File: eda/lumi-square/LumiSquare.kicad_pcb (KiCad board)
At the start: 2 copper layers, 100 x 100 mm, 70 parts, among them J1 Conn_01x02, J2 Conn_01x02, J3 Conn_01x02, J4 Conn_01x02, J5 USB_C_Receptacle_USB2.0, J6 Conn_01x04, J7 Conn_01x04, J8 Conn_01x04, J9 Conn_01x04, Q1 Q_PMOS_GSD, Q2 Q_PMOS_GSD, Q3 Q_PMOS_GSD, Q4 Q_PMOS_GSD, Q5 MMBT3904, Q6 MMBT3904, Q7 MMBT3904, Q8 MMBT3904, U1 MCP2200-I-SO, U2 ATmega1284-A, U3 ATtiny861A-S, U4 STP16CPC05MTR, U5 TPS3840, U6 TPS3840

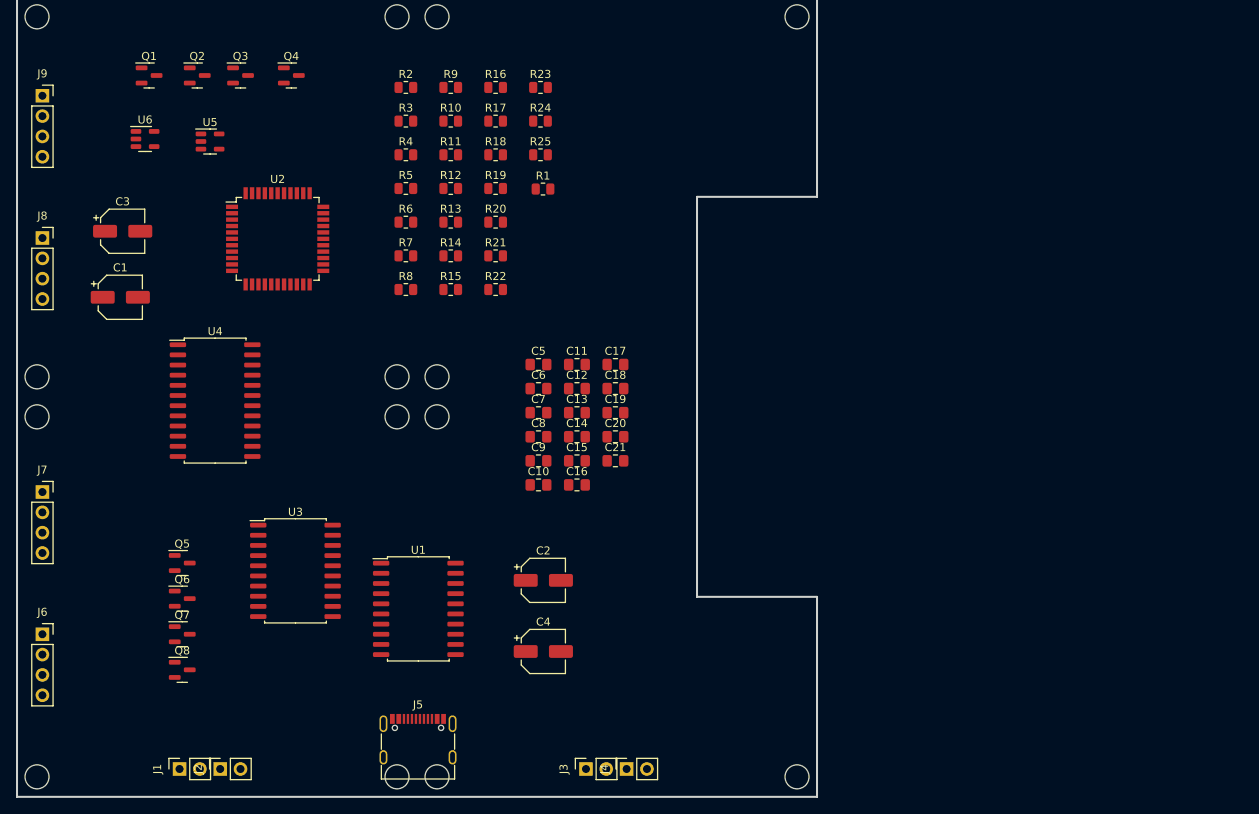
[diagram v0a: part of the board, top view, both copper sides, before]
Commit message: - Connected power portion of the schmatic - added components to the pcb editor
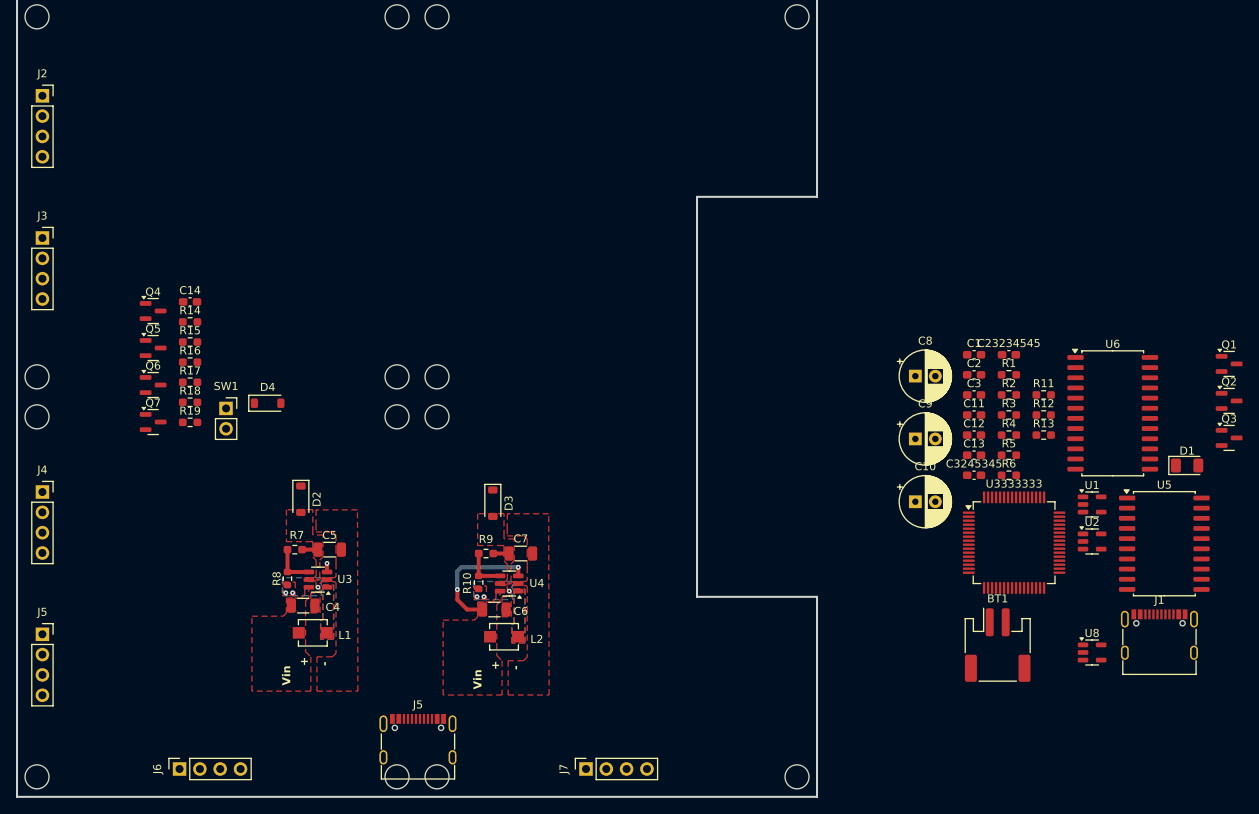
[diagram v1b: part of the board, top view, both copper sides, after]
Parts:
- removed C15, C16, C17, C18, C19, C20, C21: C, Capacitor_SMD:C_0805_2012Metric_Pad1.18x1.45mm_HandSolder
- removed the J2 at (121.9, 136.2)
- removed the J3 at (167.6, 136.2)
- removed the J4 at (172.7, 136.2)
- removed Q8: MMBT3904, Package_TO_SOT_SMD:SOT-23
- removed R20, R21, R22, R23, R24, R25: R, Resistor_SMD:R_0805_2012Metric
- added BT1: 4.2V Lipo, Connector_JST:JST_PH_S2B-PH-SM4-TB_1x02-1MP_P2.00mm_Horizontal, F.Cu at (219.1, 120.7)
- added C23234545: 1uF, Capacitor_SMD:C_0603_1608Metric_Pad1.08x0.95mm_HandSolder, F.Cu at (220.5, 84.4)
- added C3245345: 2.2uF, Capacitor_SMD:C_0603_1608Metric_Pad1.08x0.95mm_HandSolder, F.Cu at (216.2, 99.5)
- added D1: LED, LED_SMD:LED_1206_3216Metric, F.Cu at (242.8, 98.3)
- added D2: 1N5819HW-7-F, Diode_SMD:D_SOD-123, F.Cu at (132.0, 102.5)
- added D3: 1N5819HW-7-F, Diode_SMD:D_SOD-123, F.Cu at (156.0, 103.0)
- added D4: 1N4148W, Diode_SMD:D_SOD-123, F.Cu at (127.8, 90.5)
- added J6: Conn_01x04, Connector_PinSocket_2.54mm:PinSocket_1x04_P2.54mm_Vertical, F.Cu at (116.8, 136.2)
- added J7: Conn_01x04, Connector_PinSocket_2.54mm:PinSocket_1x04_P2.54mm_Vertical, F.Cu at (167.6, 136.2)
- added L1: 4.7uH, InductorCustom:Bourns SRP30xx, F.Cu at (133.5, 119.2)
- added L2: 4.7uH, InductorCustom:Bourns SRP30xx, F.Cu at (157.4, 119.7)
- added SW1: SW_Push, Connector_PinSocket_2.54mm:PinSocket_1x02_P2.54mm_Vertical, F.Cu at (122.7, 91.2)
- added U3333333: ATSAMD21J18A-A, Package_QFP:TQFP-64_10x10mm_P0.5mm, F.Cu at (221.2, 107.9)
- added U8: MIC5225-3.3YM5, Package_TO_SOT_SMD:SOT-23-5, F.Cu at (230.9, 121.7)
- C1, C2: value C_Polarized_US -> 4.7uF; footprint Capacitor_SMD:CP_Elec_5x5.3 -> Capacitor_SMD:C_0603_1608Metric_Pad1.08x0.95mm_HandSolder
- C10, C8, C9: value C -> 100uF; footprint Capacitor_SMD:C_0805_2012Metric_Pad1.18x1.45mm_HandSolder -> Capacitor_THT:CP_Radial_D6.3mm_P2.50mm
- C11, C12, C13, C14: value C -> .1uF; footprint Capacitor_SMD:C_0805_2012Metric_Pad1.18x1.45mm_HandSolder -> Capacitor_SMD:C_0603_1608Metric_Pad1.08x0.95mm_HandSolder
- C3: value C_Polarized_US -> 1uF; footprint Capacitor_SMD:CP_Elec_5x5.3 -> Capacitor_SMD:C_0603_1608Metric_Pad1.08x0.95mm_HandSolder
- C4: value C_Polarized_US -> 10uF; footprint Capacitor_SMD:CP_Elec_5x5.3 -> Capacitor_SMD:C_1206_3216Metric
- C5, C7: value C -> 22uF; footprint Capacitor_SMD:C_0805_2012Metric_Pad1.18x1.45mm_HandSolder -> Capacitor_SMD:C_1206_3216Metric
- C6: value C -> 10uF; footprint Capacitor_SMD:C_0805_2012Metric_Pad1.18x1.45mm_HandSolder -> Capacitor_SMD:C_1206_3216Metric
- J1: value Conn_01x02 -> USB_C_Receptacle_USB2.0_14P; footprint Connector_PinSocket_2.54mm:PinSocket_1x02_P2.54mm_Vertical -> Connector_USB:USB_C_Receptacle_G-Switch_GT-USB-7010ASV
- Q1: value Q_PMOS_GSD -> IRLML6244
- Q2, Q4: value Q_PMOS_GSD -> MMBT3904
- Q3: value Q_PMOS_GSD -> IRLML2246
- R1, R2: value R -> 5.1k; footprint Resistor_SMD:R_0805_2012Metric -> Resistor_SMD:R_0603_1608Metric_Pad0.98x0.95mm_HandSolder
- R10, R8: value R -> 80k; footprint Resistor_SMD:R_0805_2012Metric -> Resistor_SMD:R_0603_1608Metric
- R11: value R -> 300; footprint Resistor_SMD:R_0805_2012Metric -> Resistor_SMD:R_0603_1608Metric_Pad0.98x0.95mm_HandSolder
- R12: value R -> 100k; footprint Resistor_SMD:R_0805_2012Metric -> Resistor_SMD:R_0603_1608Metric_Pad0.98x0.95mm_HandSolder
- R13, R3: value R -> 10k; footprint Resistor_SMD:R_0805_2012Metric -> Resistor_SMD:R_0603_1608Metric_Pad0.98x0.95mm_HandSolder
- R14, R15: value R -> 200k; footprint Resistor_SMD:R_0805_2012Metric -> Resistor_SMD:R_0603_1608Metric_Pad0.98x0.95mm_HandSolder
- R16, R17, R18, R19: value R -> 2.2k; footprint Resistor_SMD:R_0805_2012Metric -> Resistor_SMD:R_0603_1608Metric_Pad0.98x0.95mm_HandSolder
- R4: value R -> 330; footprint Resistor_SMD:R_0805_2012Metric -> Resistor_SMD:R_0603_1608Metric_Pad0.98x0.95mm_HandSolder
- R5: value R -> 1.3k; footprint Resistor_SMD:R_0805_2012Metric -> Resistor_SMD:R_0603_1608Metric_Pad0.98x0.95mm_HandSolder
- R6: value R -> 150k; footprint Resistor_SMD:R_0805_2012Metric -> Resistor_SMD:R_0603_1608Metric_Pad0.98x0.95mm_HandSolder
- R7, R9: value R -> 720k; footprint Resistor_SMD:R_0805_2012Metric -> Resistor_SMD:R_0603_1608Metric_Pad0.98x0.95mm_HandSolder
- U1: value MCP2200-I-SO -> MCP73831-2-OT; footprint Package_SO:SOIC-20W_7.5x12.8mm_P1.27mm -> Package_TO_SOT_SMD:SOT-23-5
- U2: value ATmega1284-A -> TPS3840; footprint Package_QFP:TQFP-44_10x10mm_P0.8mm -> Package_TO_SOT_SMD:SOT-23-5
- U3: value ATtiny861A-S -> TLV61070A; footprint Package_SO:SOIC-20W_7.5x12.8mm_P1.27mm -> Package_TO_SOT_SMD:SOT-23-6
- U4: value STP16CPC05MTR -> TLV61070A; footprint Package_SO:SOIC-24W_7.5x15.4mm_P1.27mm -> Package_TO_SOT_SMD:SOT-23-6
- U5: value TPS3840 -> ATtiny861A-S; footprint Package_TO_SOT_SMD:SOT-23-5 -> Package_SO:SOIC-20W_7.5x12.8mm_P1.27mm
- U6: value TPS3840 -> STP16CPC05MTR; footprint Package_TO_SOT_SMD:SOT-23-5 -> Package_SO:SOIC-24W_7.5x15.4mm_P1.27mm
- moved Q1 139.7 mm to (248.0, 85.6)
- moved Q2 135.3 mm to (248.0, 90.2)
- moved Q3 131.6 mm to (248.0, 94.8)
- moved U5 129.4 mm to (239.9, 108.1)
- moved U6 125.7 mm to (233.5, 91.8)
- moved J1 123.5 mm to (239.3, 120.6), turned to 0 degrees
- moved U2 108.6 mm to (230.9, 107.8)
- moved C3 108.4 mm to (216.2, 89.5)
- moved C1 107.0 mm to (216.2, 84.4)
- moved U1 85.2 mm to (230.9, 103.2)
- moved R2 84.6 mm to (220.5, 89.5)
- moved R3 83.9 mm to (220.5, 92.0)
- moved R4 83.1 mm to (220.5, 94.5)
- moved R5 82.4 mm to (220.5, 97.0)
- moved R6 81.7 mm to (220.5, 99.5)
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- renumbered J6 to J2, J7 to J3, J8 to J4, J9 to J5
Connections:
- C1 pad 1: unconnected-(C1-Pad1) -> /5V USB
- C1 pad 2: unconnected-(C1-Pad2) -> GNDREF
- C10 pad 1: unconnected-(C10-Pad1) -> /5.3V Out
- C10 pad 2: unconnected-(C10-Pad2) -> GNDREF
- C11 pad 1: unconnected-(C11-Pad1) -> /5.3V Out
- C11 pad 2: unconnected-(C11-Pad2) -> GNDREF
- C12 pad 1: unconnected-(C12-Pad1) -> /5.3V Out
- C12 pad 2: unconnected-(C12-Pad2) -> GNDREF
- C13 pad 1: unconnected-(C13-Pad1) -> /AREF
- C13 pad 2: unconnected-(C13-Pad2) -> GNDREF
- C14 pad 1: unconnected-(C14-Pad1) -> /PB7
- C14 pad 2: unconnected-(C14-Pad2) -> GNDREF
- C2 pad 1: unconnected-(C2-Pad1) -> /4.2V Bat
- C2 pad 2: unconnected-(C2-Pad2) -> GNDREF
- C3 pad 1: unconnected-(C3-Pad1) -> /4.2V Bat
- C3 pad 2: unconnected-(C3-Pad2) -> GNDREF
- C4 pad 1: unconnected-(C4-Pad1) -> GNDREF
- C4 pad 2: unconnected-(C4-Pad2) -> /4.2V Bat
- C5 pad 1: unconnected-(C5-Pad1) -> Net-(D2-A)
- C5 pad 2: unconnected-(C5-Pad2) -> GNDREF
- C6 pad 1: unconnected-(C6-Pad1) -> /5V USB
- C6 pad 2: unconnected-(C6-Pad2) -> GNDREF
- C7 pad 1: unconnected-(C7-Pad1) -> Net-(D3-A)
- C7 pad 2: unconnected-(C7-Pad2) -> GNDREF
- C8 pad 1: unconnected-(C8-Pad1) -> /5.3V Out
- C8 pad 2: unconnected-(C8-Pad2) -> GNDREF
- C9 pad 1: unconnected-(C9-Pad1) -> /5.3V Out
- C9 pad 2: unconnected-(C9-Pad2) -> GNDREF
- J2 pad 2: unconnected-(J6-Pin_2-Pad2) -> /LED1
- J2 pad 3: unconnected-(J6-Pin_3-Pad3) -> /LED2
- J2 pad 4: unconnected-(J6-Pin_4-Pad4) -> /LED3
- J3 pad 2: unconnected-(J7-Pin_2-Pad2) -> /LED4
- J3 pad 3: unconnected-(J7-Pin_3-Pad3) -> /LED5
- J3 pad 4: unconnected-(J7-Pin_4-Pad4) -> /LED6
- J4 pad 2: unconnected-(J8-Pin_2-Pad2) -> /LED7
- J4 pad 3: unconnected-(J8-Pin_3-Pad3) -> /LED8
- J4 pad 4: unconnected-(J8-Pin_4-Pad4) -> /LED9
- J5 pad 2: unconnected-(J9-Pin_2-Pad2) -> /LED10
- J5 pad 3: unconnected-(J9-Pin_3-Pad3) -> /LED11
- J5 pad 4: unconnected-(J9-Pin_4-Pad4) -> /LED12
- Q1 pad 1: unconnected-(Q1-G-Pad1) -> /5V USB
- Q1 pad 2: unconnected-(Q1-S-Pad2) -> GNDREF
- Q1 pad 3: unconnected-(Q1-D-Pad3) -> Net-(Q1-D)
- Q2 pad 1: unconnected-(Q2-G-Pad1) -> Net-(Q2-B)
- Q2 pad 2: unconnected-(Q2-S-Pad2) -> GNDREF
- Q2 pad 3: unconnected-(Q2-D-Pad3) -> Net-(Q2-C)
- Q3 pad 1: unconnected-(Q3-G-Pad1) -> Net-(Q2-C)
- Q3 pad 2: unconnected-(Q3-S-Pad2) -> /5.3V Out
- Q3 pad 3: unconnected-(Q3-D-Pad3) -> Net-(Q3-D)
- R1 pad 1: unconnected-(R1-Pad1) -> Net-(J1-CC2)
- R1 pad 2: unconnected-(R1-Pad2) -> GNDREF
- R10 pad 1: unconnected-(R10-Pad1) -> Net-(U4-FB)
- R10 pad 2: unconnected-(R10-Pad2) -> GNDREF
- R11 pad 1: unconnected-(R11-Pad1) -> Net-(U5-PA7)
- R11 pad 2: unconnected-(R11-Pad2) -> Net-(Q2-B)
- R12 pad 1: unconnected-(R12-Pad1) -> Net-(U5-PA7)
- R12 pad 2: unconnected-(R12-Pad2) -> GNDREF
- R13 pad 1: unconnected-(R13-Pad1) -> /5.3V Out
- R13 pad 2: unconnected-(R13-Pad2) -> Net-(Q2-C)
- R14 pad 1: unconnected-(R14-Pad1) -> /5.3V Out
- R14 pad 2: unconnected-(R14-Pad2) -> /PB6
- R15 pad 1: unconnected-(R15-Pad1) -> /5.3V Out
- R15 pad 2: unconnected-(R15-Pad2) -> /PB7
- R2 pad 1: unconnected-(R2-Pad1) -> Net-(J1-CC1)
- R2 pad 2: unconnected-(R2-Pad2) -> GNDREF
- R3 pad 1: unconnected-(R3-Pad1) -> Net-(U1-PROG)
- R3 pad 2: unconnected-(R3-Pad2) -> GNDREF
- R4 pad 1: unconnected-(R4-Pad1) -> /5V USB
- R4 pad 2: unconnected-(R4-Pad2) -> Net-(D1-A)
- R5 pad 1: unconnected-(R5-Pad1) -> /5V USB
- R5 pad 2: unconnected-(R5-Pad2) -> GNDREF
- R6 pad 1: unconnected-(R6-Pad1) -> /4.2V Bat
- R6 pad 2: unconnected-(R6-Pad2) -> Net-(Q1-D)
- R7 pad 1: unconnected-(R7-Pad1) -> Net-(D2-A)
- R7 pad 2: unconnected-(R7-Pad2) -> Net-(U3-FB)
- R8 pad 1: unconnected-(R8-Pad1) -> Net-(U3-FB)
- R8 pad 2: unconnected-(R8-Pad2) -> GNDREF
- R9 pad 1: unconnected-(R9-Pad1) -> Net-(D3-A)
- R9 pad 2: unconnected-(R9-Pad2) -> Net-(U4-FB)
- U1 pad 1: unconnected-(U1-VDD-Pad1) -> Net-(D1-K)
- U1 pad 2: unconnected-(U1-OSC1-Pad2) -> GNDREF
- U1 pad 3: unconnected-(U1-OSC2-Pad3) -> /4.2V Bat
- U1 pad 4: unconnected-(U1-RST-Pad4) -> /5V USB
- U1 pad 5: unconnected-(U1-GP7/TxLED-Pad5) -> Net-(U1-PROG)
- U2 pad 1: unconnected-(U2-PB5-Pad1) -> Net-(Q1-D)
- U2 pad 2: unconnected-(U2-PB6-Pad2) -> /4.2V Bat
- U2 pad 3: unconnected-(U2-PB7-Pad3) -> GNDREF
- U2 pad 5: Net-(U2-VCC-Pad17) -> unconnected-(U2-CT-Pad5)
- U3 pad 1: unconnected-(U3-PB0-Pad1) -> Net-(U3-SW)
- U3 pad 2: unconnected-(U3-PB1-Pad2) -> GNDREF
- U3 pad 3: unconnected-(U3-PB2-Pad3) -> Net-(Q1-D)
- U3 pad 4: unconnected-(U3-PB3-Pad4) -> Net-(U3-FB)
- U3 pad 5: unconnected-(U3-VCC-Pad5) -> Net-(D2-A)
- U3 pad 6: unconnected-(U3-GND-Pad6) -> /4.2V Bat
- U4 pad 1: unconnected-(U4-GND-Pad1) -> Net-(U4-SW)
- U4 pad 2: unconnected-(U4-SIN-Pad2) -> GNDREF
- U4 pad 3: unconnected-(U4-CLK-Pad3) -> /5V USB
- U4 pad 4: unconnected-(U4-LATCH-Pad4) -> Net-(U4-FB)
- U4 pad 5: unconnected-(U4-LED1-Pad5) -> Net-(D3-A)
- U4 pad 6: unconnected-(U4-LED2-Pad6) -> /5V USB
- U5 pad 5: unconnected-(U5-CT-Pad5) -> /5.3V Out
- U6 pad 5: unconnected-(U6-CT-Pad5) -> /LED1
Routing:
- net /5V USB: track 0.00 -> 16.1 mm, vias 0 -> 2
- net Net-(U4-FB): track 0.00 -> 5.48 mm
- net Net-(U3-FB): track 0.00 -> 5.48 mm
- net Net-(D3-A): track 0.00 -> 1.96 mm
- net Net-(D2-A): track 0.00 -> 1.96 mm
- net Net-(Q1-D): track 0.00 -> 1.08 mm
- net GNDREF: vias 0 -> 6
- net (no net): vias 0 -> 1
- added copper zone on B.Cu, net (none)
- added copper zone on F.Cu, net (none)
- added copper zone on F.Cu, net /4.2V Bat
- added copper zone on F.Cu, net /5V USB
- added copper zone on B.Cu, net GNDREF
- added copper zone on F.Cu, net GNDREF
- added copper zone on F.Cu, net Net-(D2-A)
- added copper zone on F.Cu, net Net-(D3-A)
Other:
- board text added: "+"
- board text added: "-"
- board text added: "Vin"

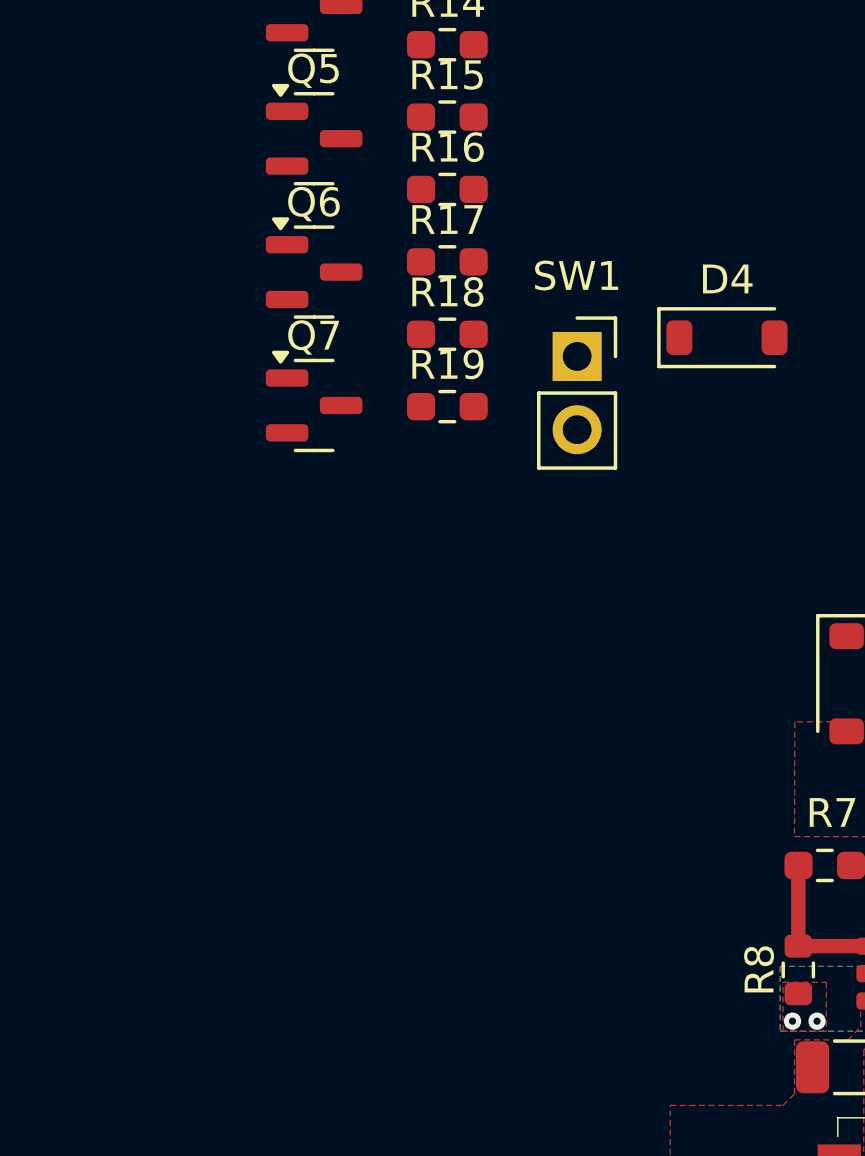
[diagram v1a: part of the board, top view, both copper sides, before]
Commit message: - Made updates to LumiSquare pcb and schematic
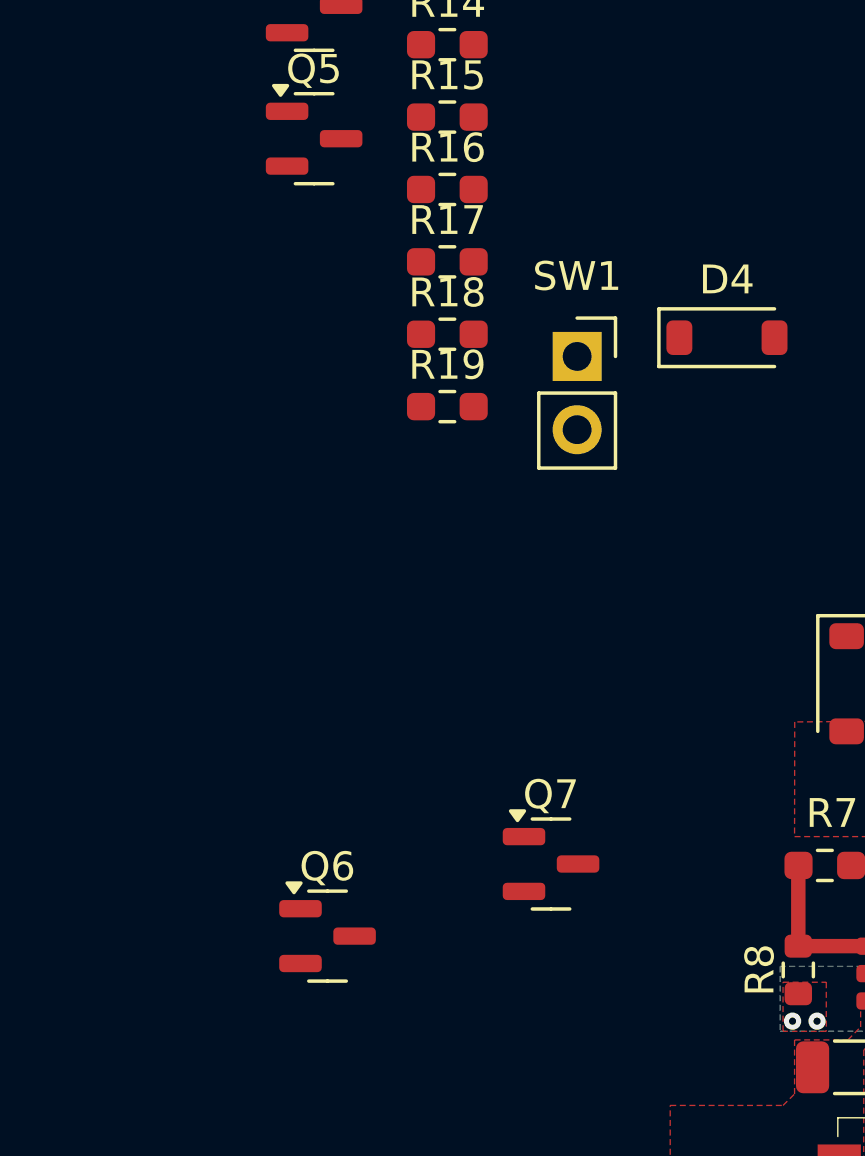
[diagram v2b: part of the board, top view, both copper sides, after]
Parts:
- moved Q6 23.0 mm to (114.0, 111.2)
- moved Q7 17.9 mm to (121.8, 108.8)
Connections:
- net /LED1 renamed Net-(J2-Pin_2)
- net /LED10 renamed Net-(J5-Pin_2)
- net /LED11 renamed Net-(J5-Pin_3)
- net /LED12 renamed Net-(J5-Pin_4)
- net /LED2 renamed Net-(J2-Pin_3)
- net /LED3 renamed Net-(J2-Pin_4)
- net /LED4 renamed Net-(J3-Pin_2)
- net /LED5 renamed Net-(J3-Pin_3)
- net /LED6 renamed Net-(J3-Pin_4)
- net /LED7 renamed Net-(J4-Pin_2)
- net /LED8 renamed Net-(J4-Pin_3)
- net /LED9 renamed Net-(J4-Pin_4)
- J2 pad 1: unconnected-(J2-Pin_1-Pad1) -> /Matrix Switch 1
- J3 pad 1: unconnected-(J3-Pin_1-Pad1) -> /Matrix Switch 2
- J4 pad 1: unconnected-(J4-Pin_1-Pad1) -> /Matrix Switch 3
- J5 pad 1: unconnected-(J5-Pin_1-Pad1) -> /Matrix Switch 4
- J6 pad 1: unconnected-(J6-Pin_1-Pad1) -> Net-(J6-Pin_1)
- J6 pad 3: unconnected-(J6-Pin_3-Pad3) -> Net-(J6-Pin_3)
- J7 pad 1: unconnected-(J7-Pin_1-Pad1) -> Net-(J7-Pin_1)
- J7 pad 3: unconnected-(J7-Pin_3-Pad3) -> Net-(J7-Pin_3)
- Q4 pad 1: unconnected-(Q4-B-Pad1) -> Net-(Q4-B)
- Q4 pad 2: unconnected-(Q4-E-Pad2) -> Net-(J6-Pin_1)
- Q4 pad 3: unconnected-(Q4-C-Pad3) -> /5.3V Out
- Q5 pad 1: unconnected-(Q5-B-Pad1) -> Net-(Q5-B)
- Q5 pad 2: unconnected-(Q5-E-Pad2) -> Net-(J6-Pin_3)
- Q5 pad 3: unconnected-(Q5-C-Pad3) -> /5.3V Out
- Q6 pad 1: unconnected-(Q6-B-Pad1) -> Net-(Q6-B)
- Q6 pad 2: unconnected-(Q6-E-Pad2) -> Net-(J7-Pin_1)
- Q6 pad 3: unconnected-(Q6-C-Pad3) -> /5.3V Out
- Q7 pad 1: unconnected-(Q7-B-Pad1) -> Net-(Q7-B)
- Q7 pad 2: unconnected-(Q7-E-Pad2) -> Net-(J7-Pin_3)
- Q7 pad 3: unconnected-(Q7-C-Pad3) -> /5.3V Out
- R16 pad 2: unconnected-(R16-Pad2) -> Net-(Q4-B)
- R17 pad 2: unconnected-(R17-Pad2) -> Net-(Q5-B)
- R18 pad 2: unconnected-(R18-Pad2) -> Net-(Q6-B)
- R19 pad 2: unconnected-(R19-Pad2) -> Net-(Q7-B)
- U3333333 pad 11: unconnected-(U3333333-PB08-Pad11) -> /Matrix Switch 1
- U3333333 pad 12: unconnected-(U3333333-PB09-Pad12) -> /Matrix Switch 2
- U3333333 pad 23: unconnected-(U3333333-PB10-Pad23) -> /Matrix Switch 3
- U3333333 pad 24: unconnected-(U3333333-PB11-Pad24) -> /Matrix Switch 4
- U6 pad 1: unconnected-(U6-GND-Pad1) -> GNDREF
- U6 pad 24: unconnected-(U6-VDD-Pad24) -> +3.3V Main

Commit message: Adding button matrix kicad project- - Used dma to send audio usart data for samd21
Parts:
- removed C11, C12, C13, C14: .1uF, Capacitor_SMD:C_0603_1608Metric_Pad1.08x0.95mm_HandSolder
- removed D4: 1N4148W, Diode_SMD:D_SOD-123
- removed Q2: MMBT3904, Package_TO_SOT_SMD:SOT-23
- removed R14, R15: 200k, Resistor_SMD:R_0603_1608Metric_Pad0.98x0.95mm_HandSolder
- removed SW1: SW_Push, Connector_PinSocket_2.54mm:PinSocket_1x02_P2.54mm_Vertical
- removed U5: ATtiny861A-S, Package_SO:SOIC-20W_7.5x12.8mm_P1.27mm
- moved C10 192.1 mm to (17.5, 85.0)
- moved C8 192.1 mm to (17.5, 69.3)
- moved C9 192.1 mm to (17.5, 77.2)
- moved BT1 182.5 mm to (36.6, 117.1)
- moved J1 179.3 mm to (60.0, 120.0)
- moved U6 171.5 mm to (62.9, 75.0)
- moved C1 171.5 mm to (45.5, 67.7)
- moved C2 171.5 mm to (45.5, 70.2)
- moved C23234545 171.5 mm to (49.9, 67.7)
- moved C3 171.5 mm to (45.5, 72.7)
- moved C3245345 171.5 mm to (45.5, 82.7)
- moved D1 171.5 mm to (72.2, 81.5)
- moved Q1 171.5 mm to (77.4, 68.8)
- moved Q3 171.5 mm to (77.4, 78.1)
- moved R1 171.5 mm to (49.9, 70.2)
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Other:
- board size 100 x 100 mm -> 166.5 x 100 mm
